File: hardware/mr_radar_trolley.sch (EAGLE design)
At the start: 42 parts, among them IC1 AD711RN, IC2 REG1117, IC3 REG1117, IC4 LM2940, U1 FT232RL-BASICSSOP

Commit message: finished component placement draft on mr_radar_trolley
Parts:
- JP5, JP9: device SparkFun-Connectors:M08LOCK -> SparkFun-Connectors:M05LOCK
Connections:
- net +3V3: now also C3.+
- net GND: no longer JP5.6, JP5.7, JP5.8, JP9.6, JP9.7, JP9.8

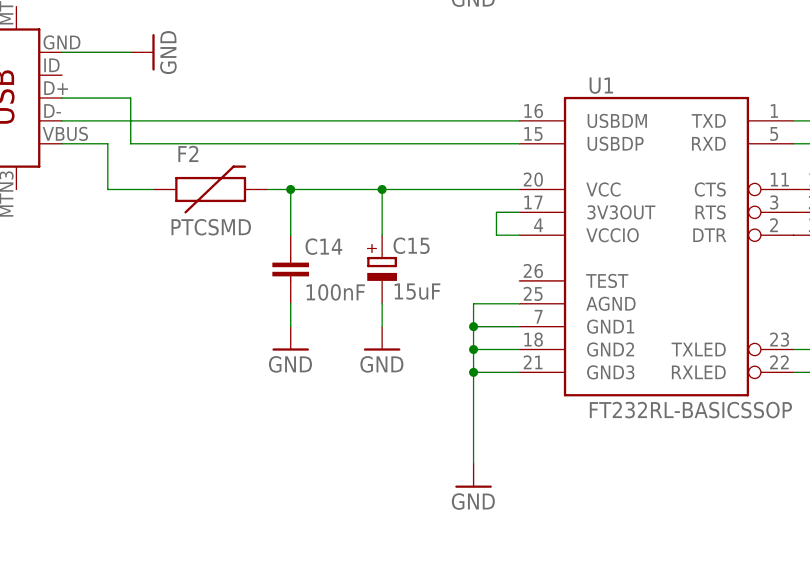
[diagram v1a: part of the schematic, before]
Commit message: fixes to ft232rl layout and schematic, cleanup of silkscreen layer, sent for manufacturing
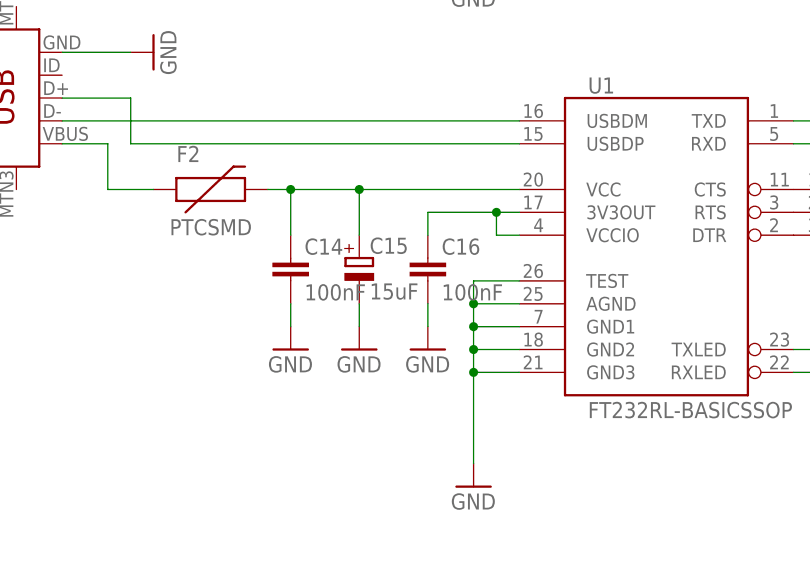
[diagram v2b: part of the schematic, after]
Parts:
- added C16: 100nF, resistor:C-EUC0603
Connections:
- net GND: now also C16.2, U1.TEST
- net N$7: now also C16.1
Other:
- moved on the sheet: C15
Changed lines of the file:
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@@
 <part name="JP5" library="SparkFun-Connectors" deviceset="M05" device="LOCK"/>
 <part name="JP9" library="SparkFun-Connectors" deviceset="M05" device="LOCK"/>
+<part name="C16" library="resistor" deviceset="C-EU" device="C0603" value="100nF"/>
+<part name="GND30" library="SparkFun-Aesthetics" deviceset="GND" device=""/>
 </parts>
 <sheets>
@@
 <instance part="C14" gate="G$1" x="2.54" y="93.98"/>
 <instance part="GND24" gate="1" x="2.54" y="83.82"/>
-<instance part="C15" gate="G$1" x="12.7" y="93.98"/>
-<instance part="GND25" gate="1" x="12.7" y="83.82"/>
+<instance part="C15" gate="G$1" x="10.16" y="93.98"/>
+<instance part="GND25" gate="1" x="10.16" y="83.82"/>
 <instance part="JP7" gate="G$1" x="66.04" y="99.06" rot="R180"/>
 <instance part="FRAME1" gate="G$1" x="-38.1" y="40.64"/>
@@
 <instance part="JP5" gate="G$1" x="203.2" y="116.84" rot="R180"/>
 <instance part="JP9" gate="G$1" x="106.68" y="165.1" rot="R180"/>
+<instance part="C16" gate="G$1" x="17.78" y="93.98"/>
+<instance part="GND30" gate="1" x="17.78" y="83.82"/>
 </instances>
 <busses>
@@
 <wire x1="27.94" y1="81.28" x2="22.86" y2="81.28" width="0.1524" layer="91"/>
 <junction x="22.86" y="81.28"/>
+<pinref part="U1" gate="G$1" pin="TEST"/>
+<wire x1="27.94" y1="91.44" x2="22.86" y2="91.44" width="0.1524" layer="91"/>
+<wire x1="22.86" y1="91.44" x2="22.86" y2="88.9" width="0.1524" layer="91"/>
+<junction x="22.86" y="88.9"/>
 </segment>
 <segment>
@@
 <pinref part="GND25" gate="1" pin="GND"/>
 <pinref part="C15" gate="G$1" pin="-"/>
-<wire x1="12.7" y1="86.36" x2="12.7" y2="88.9" width="0.1524" layer="91"/>
+<wire x1="10.16" y1="86.36" x2="10.16" y2="88.9" width="0.1524" layer="91"/>
 </segment>
 <segment>
@@
 <pinref part="JP9" gate="G$1" pin="4"/>
 <pinref part="JP9" gate="G$1" pin="5"/>
+</segment>
+<segment>
+<pinref part="C16" gate="G$1" pin="2"/>
+<pinref part="GND30" gate="1" pin="GND"/>
+<wire x1="17.78" y1="88.9" x2="17.78" y2="86.36" width="0.1524" layer="91"/>
 </segment>
 </net>
@@
 <wire x1="27.94" y1="99.06" x2="25.4" y2="99.06" width="0.1524" layer="91"/>
 <wire x1="25.4" y1="99.06" x2="25.4" y2="96.52" width="0.1524" layer="91"/>
+<pinref part="C16" gate="G$1" pin="1"/>
+<wire x1="25.4" y1="99.06" x2="17.78" y2="99.06" width="0.1524" layer="91"/>
+<wire x1="17.78" y1="99.06" x2="17.78" y2="96.52" width="0.1524" layer="91"/>
+<junction x="25.4" y="99.06"/>
 </segment>
 </net>
@@
 <wire x1="0" y1="101.6" x2="2.54" y2="101.6" width="0.1524" layer="91"/>
 <pinref part="C14" gate="G$1" pin="1"/>
-<wire x1="2.54" y1="101.6" x2="12.7" y2="101.6" width="0.1524" layer="91"/>
-<wire x1="12.7" y1="101.6" x2="27.94" y2="101.6" width="0.1524" layer="91"/>
+<wire x1="2.54" y1="101.6" x2="10.16" y2="101.6" width="0.1524" layer="91"/>
+<wire x1="10.16" y1="101.6" x2="27.94" y2="101.6" width="0.1524" layer="91"/>
 <wire x1="2.54" y1="96.52" x2="2.54" y2="101.6" width="0.1524" layer="91"/>
 <junction x="2.54" y="101.6"/>
 <pinref part="C15" gate="G$1" pin="+"/>
-<wire x1="12.7" y1="96.52" x2="12.7" y2="101.6" width="0.1524" layer="91"/>
-<junction x="12.7" y="101.6"/>
+<wire x1="10.16" y1="96.52" x2="10.16" y2="101.6" width="0.1524" layer="91"/>
+<junction x="10.16" y="101.6"/>
 </segment>
 </net>
@@
 </sheet>
 </sheets>
+<errors>
+</errors>
 </schematic>
 </drawing>
